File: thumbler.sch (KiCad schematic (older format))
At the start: 255 parts, among them J1 USB_B_Micro, J2 Conn_01x04, J3 Conn_01x04, J4 DIN-5_180degree, J5 Conn_01x04, J6 DIN-5_180degree, J7 Conn_01x04, J8 USB_B_Micro, SW1 SW_Push, SW2 SW_DIP_x05, SW3 SW_Push, SW4 SW_DIP_x05, U1 STM32F072C8Tx, U2 MCP1700-3302E_SOT89, U3 MCP1700-3302E_SOT89, U4 STM32F072C8Tx, X1 ENCODER_ANO

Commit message: 70 key laid out
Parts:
- added J?: Conn_01x08, symbol Connector_Generic:Conn_01x08
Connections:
- net GND: now also J?.1 (Pin_1)
- net L_ENC_A: now also J?.8 (Pin_8)
- net L_ENC_B: now also J?.7 (Pin_7)
- net L_ENC_BN: now also J?.6 (Pin_6)
- net L_ENC_DN: now also J?.5 (Pin_5)
- net L_ENC_LF: now also J?.2 (Pin_2)
- net L_ENC_RT: now also J?.4 (Pin_4)
- net L_ENC_UP: now also J?.3 (Pin_3)
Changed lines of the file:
@@
 	9750 10100 9750 10150
 Wire Notes Line
-	11200 11900 7550 11900
-Wire Notes Line
-	7550 9600 7550 11900
+	6500 9600 6500 11900
 Wire Notes Line
 	11200 5550 11200 11900
@@
 	19100 8200 19100 8700
 Connection ~ 19100 8200
+$Comp
+L Connector_Generic:Conn_01x08 J?
+U 1 1 6D7D2149
+P 6900 10950
+F 0 "J?" H 6818 10325 50  0000 C CNN
+F 1 "Conn_01x08" H 6818 10416 50  0000 C CNN
+F 2 "" H 6900 10950 50  0001 C CNN
+F 3 "~" H 6900 10950 50  0001 C CNN
+	1    6900 10950
+	-1   0    0    1
+$EndComp
+Text GLabel 7100 10550 2    50   Input ~ 0
+L_ENC_A
+Text GLabel 7100 10650 2    50   Input ~ 0
+L_ENC_B
+Text GLabel 7100 10750 2    50   Input ~ 0
+L_ENC_BN
+Text GLabel 7100 10850 2    50   Input ~ 0
+L_ENC_DN
+Text GLabel 7100 11050 2    50   Input ~ 0
+L_ENC_UP
+Text GLabel 7100 11150 2    50   Input ~ 0
+L_ENC_LF
+Text GLabel 7100 10950 2    50   Input ~ 0
+L_ENC_RT
+$Comp
+L power:GND #PWR?
+U 1 1 6DC33371
+P 7150 11300
+F 0 "#PWR?" H 7150 11050 50  0001 C CNN
+F 1 "GND" H 7155 11127 50  0000 C CNN
+F 2 "" H 7150 11300 50  0001 C CNN
+F 3 "" H 7150 11300 50  0001 C CNN
+	1    7150 11300
+	1    0    0    -1
+$EndComp
+Wire Wire Line
+	7100 11250 7150 11250
+Wire Wire Line
+	7150 11250 7150 11300
+Wire Notes Line
+	11200 11900 6500 11900
 $EndSCHEMATC

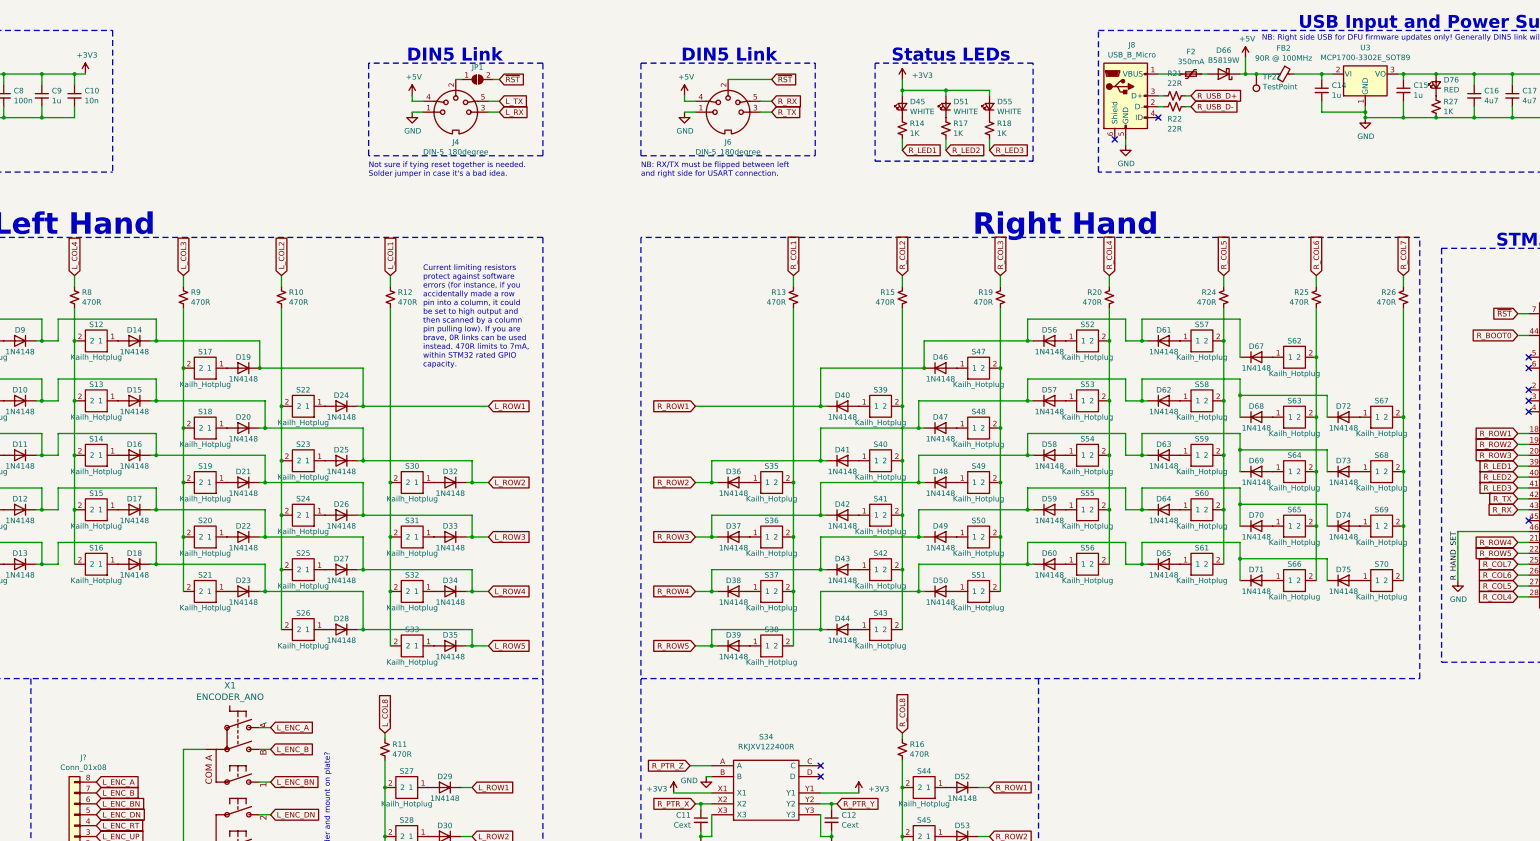
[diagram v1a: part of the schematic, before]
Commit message: left mostly routed; kicad 6; need to cleanup files...
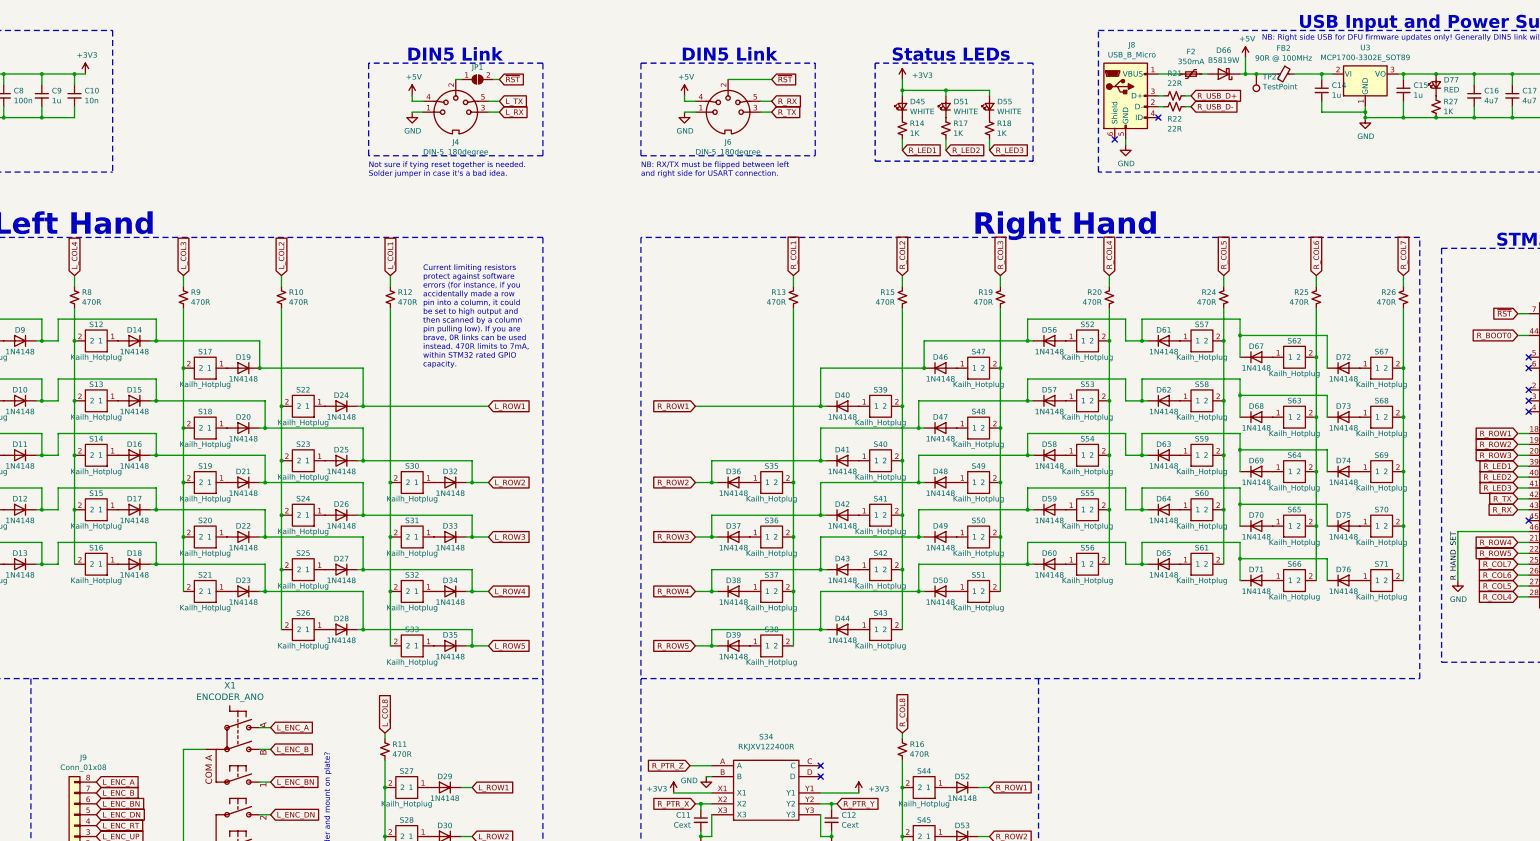
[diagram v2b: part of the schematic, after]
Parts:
- added D72: 1N4148, Diode_THT:D_DO-35_SOD27_P7.62mm_Horizontal, symbol Diode:1N4148
- added S67: Kailh_Hotplug, keyswitches:Kailh_socket_MX_platemount, symbol kailh_hotplug_mx_plate:Kailh_Hotplug
- J9: renamed from J?; footprint (none) -> Connector_PinHeader_2.54mm:PinHeader_2x04_P2.54mm_Vertical
- renumbered D72 to D73, D73 to D74, D74 to D75, D75 to D76, D76 to D77, S67 to S68, S68 to S69, S69 to S70, S70 to S71
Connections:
- net R_ROW1: now also D72.1 (K)
- net at R26.2, S68.2, S69.2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: now also S67.2
- net ~RST renamed ~{RST}
- new net: D72.2 (A), S67.1
